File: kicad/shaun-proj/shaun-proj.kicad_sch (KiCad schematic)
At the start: 64 parts, among them J1 USB_C_Receptacle_USB2.0_16P, J2 Conn_02x16_Odd_Even, J3 Conn_01x02_Socket, Q1 AO3401A, Q2 AO3400A, Q3 AO3401A, Q4 AO3400A, Q5 AO3400A, Q6 AO3401A, SW2 SW_SPDT, U1 CH224K, U2 TPS5430DDA, U3 INA219AxD, U5 TP4056-42-ESOP8

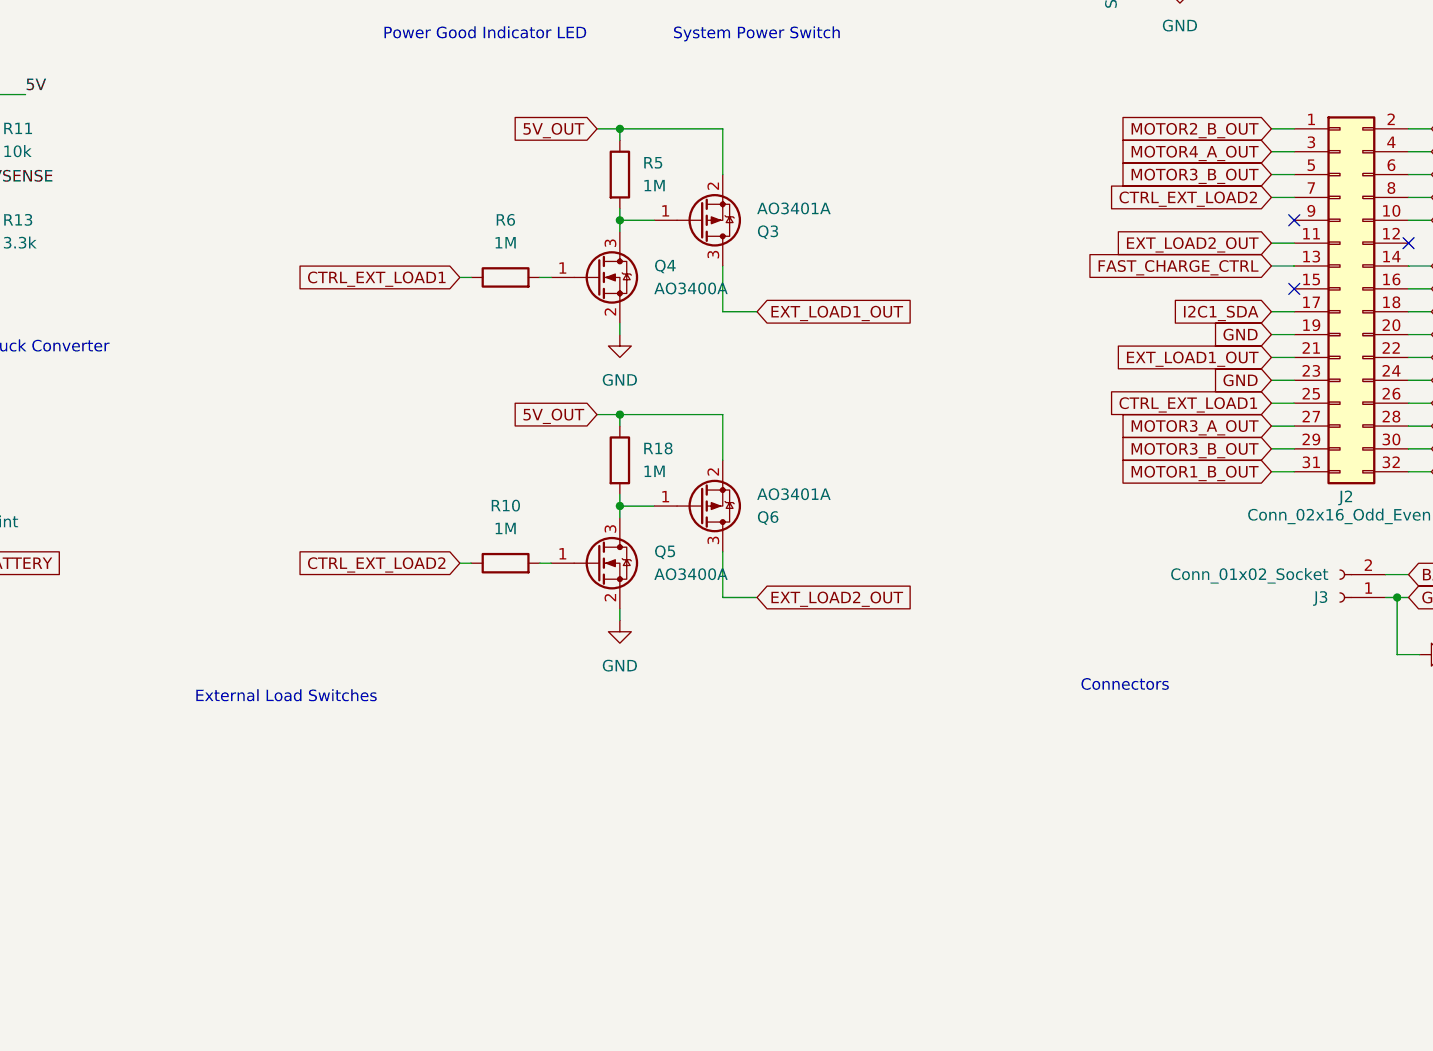
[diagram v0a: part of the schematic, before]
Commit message: combine schematics, optimize damolas schematic, fixes, part assignment, pcb population
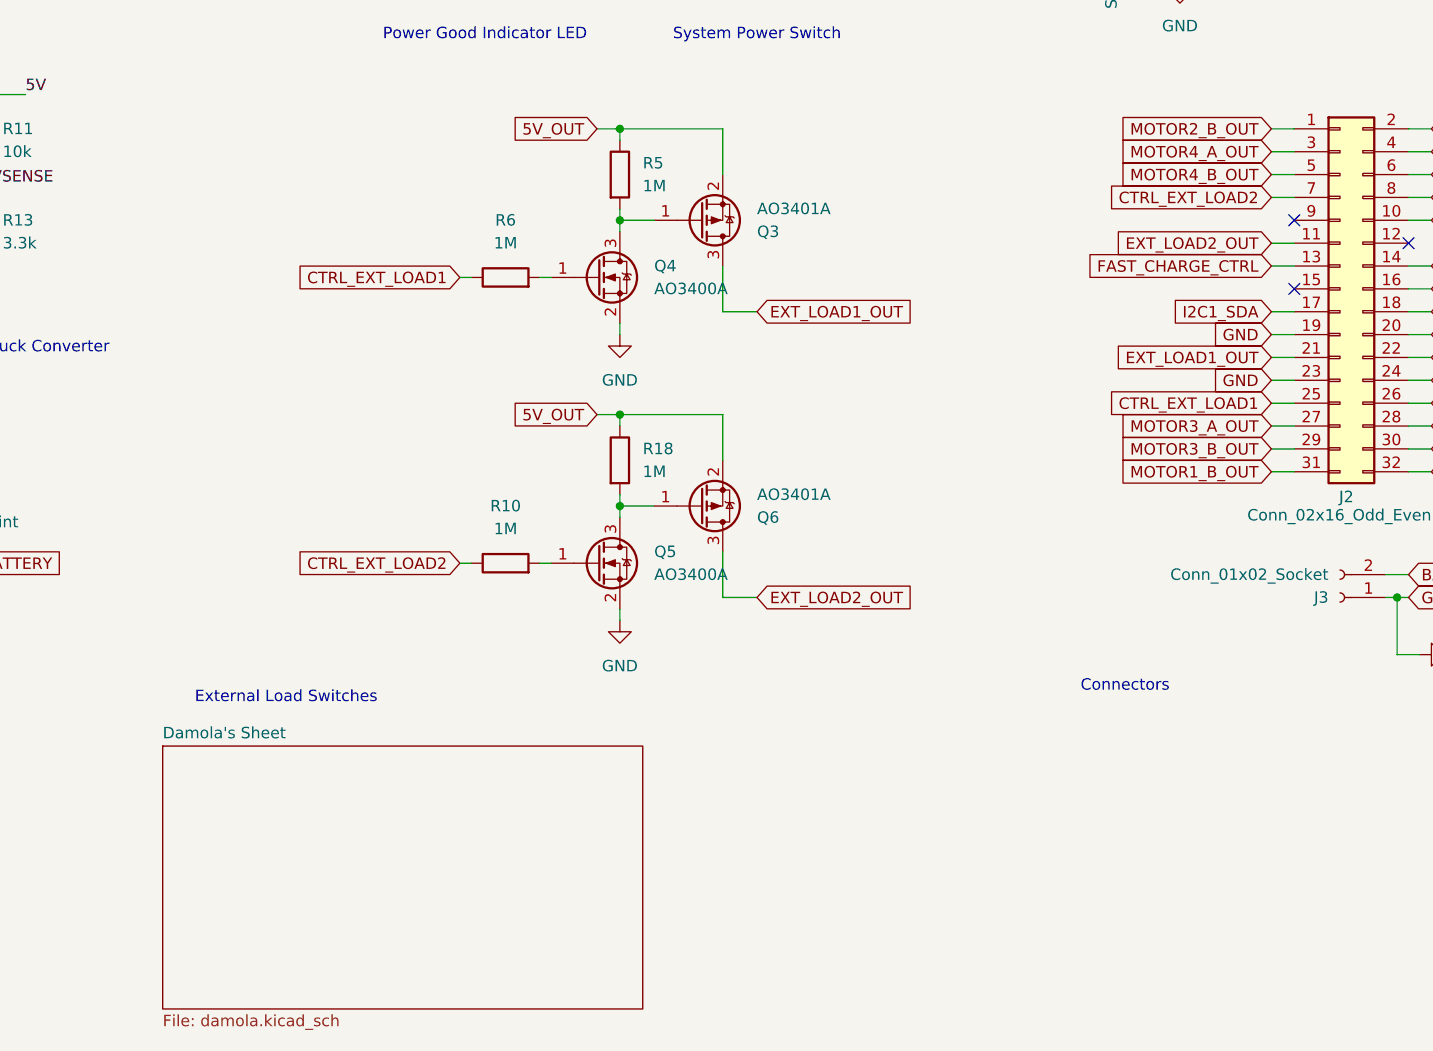
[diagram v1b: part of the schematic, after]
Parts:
- R10, R18, R3, R5, R6: footprint Resistor_SMD:R_0603_1608Metric -> Resistor_SMD:R_0603_1608Metric_Pad0.98x0.95mm_HandSolder
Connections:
- net MOTOR3_B_OUT: no longer J2.5 (Pin_5)
- new net MOTOR4_B_OUT: J2.5 (Pin_5)
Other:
- added sheet Damola's Sheet (damola.kicad_sch)
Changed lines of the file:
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@@
 		)
 	)
-	(global_label "MOTOR3_B_OUT"
+	(global_label "MOTOR4_B_OUT"
 		(shape input)
 		(at 243.84 102.87 180)
@@
 		(polyline
 			(pts
-				(xy 13.97 81.28) (xy 118.11 81.28) (xy 118.11 13.97) (xy 13.97 13.97)
+				(xy 13.97 128.27) (xy 118.11 128.27) (xy 118.11 195.58) (xy 13.97 195.58)
 			)
 			(stroke
@@
 		(polyline
 			(pts
-				(xy 171.45 59.69) (xy 120.65 59.69) (xy 120.65 13.97) (xy 171.45 13.97)
+				(xy 173.99 59.69) (xy 283.21 59.69) (xy 283.21 13.97) (xy 189.23 13.97) (xy 173.99 13.97)
 			)
 			(stroke
@@
 		(polyline
 			(pts
-				(xy 13.97 125.73) (xy 118.11 125.73) (xy 118.11 83.82) (xy 13.97 83.82)
+				(xy 171.45 59.69) (xy 120.65 59.69) (xy 120.65 13.97) (xy 171.45 13.97)
 			)
 			(stroke
@@
 		(polyline
 			(pts
-				(xy 13.97 128.27) (xy 118.11 128.27) (xy 118.11 195.58) (xy 13.97 195.58)
+				(xy 13.97 125.73) (xy 118.11 125.73) (xy 118.11 83.82) (xy 13.97 83.82)
 			)
 			(stroke
@@
 		(polyline
 			(pts
-				(xy 173.99 59.69) (xy 283.21 59.69) (xy 283.21 13.97) (xy 189.23 13.97) (xy 173.99 13.97)
+				(xy 13.97 81.28) (xy 118.11 81.28) (xy 118.11 13.97) (xy 13.97 13.97)
 			)
 			(stroke
@@
 			)
 		)
-		(property "Footprint" "Resistor_SMD:R_0603_1608Metric"
+		(property "Footprint" "Resistor_SMD:R_0603_1608Metric_Pad0.98x0.95mm_HandSolder"
 			(at 169.672 134.62 90)
 			(effects
@@
 			)
 		)
-		(property "Footprint" "Resistor_SMD:R_0603_1608Metric"
+		(property "Footprint" "Resistor_SMD:R_0603_1608Metric_Pad0.98x0.95mm_HandSolder"
 			(at 169.672 102.87 90)
 			(effects
@@
 			)
 		)
-		(property "Footprint" "Resistor_SMD:R_0603_1608Metric"
+		(property "Footprint" "Resistor_SMD:R_0603_1608Metric_Pad0.98x0.95mm_HandSolder"
 			(at 125.222 30.48 90)
 			(effects
@@
 			)
 		)
-		(property "Footprint" "Resistor_SMD:R_0603_1608Metric"
+		(property "Footprint" "Resistor_SMD:R_0603_1608Metric_Pad0.98x0.95mm_HandSolder"
 			(at 158.75 116.078 90)
 			(effects
@@
 			)
 		)
-		(property "Footprint" "Resistor_SMD:R_0603_1608Metric"
+		(property "Footprint" "Resistor_SMD:R_0603_1608Metric_Pad0.98x0.95mm_HandSolder"
 			(at 158.75 147.828 90)
 			(effects
@@
 				)
 			)
+		)
+	)
+	(sheet
+		(at 120.65 166.37)
+		(size 53.34 29.21)
+		(exclude_from_sim no)
+		(in_bom yes)
+		(on_board yes)
+		(dnp no)
+		(fields_autoplaced yes)
+		(stroke
+			(width 0.1524)
+			(type solid)
+		)
+		(fill
+			(color 0 0 0 0.0000)
+		)
+		(property "Sheetname" "Damola's Sheet"
+			(at 120.65 165.6584 0)
+			(effects
+				(font
+					(size 1.27 1.27)
+				)
+				(justify left bottom)
+			)
+		)
+		(property "Sheetfile" "damola.kicad_sch"
+			(at 120.65 196.1646 0)
+			(effects
+				(font
+					(size 1.27 1.27)
+				)
+				(justify left top)
+			)
+		)
+		(instances
+			(project "shaun-proj"
+				(path "/dda18d53-e032-419d-b3dd-4e5b9f14d709"
+					(page "2")
+				)
+			)

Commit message: da board
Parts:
- removed C7: 100n, Capacitor_SMD:C_0603_1608Metric_Pad1.08x0.95mm_HandSolder, symbol Device:C
- removed TP13, TP4, TP5, TP9: TestPoint, TestPoint:TestPoint_Pad_D1.5mm, symbol Connector:TestPoint
- added H1: MountingHole, MountingHole:MountingHole_3.2mm_M3, symbol Mechanical:MountingHole
- R10, R6: value 1M -> 10k
- R4: value 560 -> 2k
- SW2: JLC (none) -> https://jlcpcb.com/partdetail/XkbConnection-SS12D11G3R/C843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
- U1: footprint Package_SO:SSOP-10-1EP_3.9x4.9mm_P1mm_EP2.1x3.3mm -> Package_SO:SSOP-10-1EP_3.9x4.9mm_P1mm_EP2.1x3.3mm_ThermalVias
- U5: footprint Package_SO:SOIC-8-1EP_3.9x4.9mm_P1.27mm_EP2.41x3.3mm -> Package_SO:SOIC-8-1EP_3.9x4.9mm_P1.27mm_EP2.41x3.3mm_ThermalVias; LCSC C9864 -> C16581
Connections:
- net 3V3_OUT: now also J2.17 (Pin_17); no longer J2.18 (Pin_18), R12.1, TP11.1
- net 5V_OUT: now also J2.19 (Pin_19); no longer J2.20 (Pin_20)
- net BATTERY: now also J2.13 (Pin_13), SW2.2 (B); no longer C5.1, J2.14 (Pin_14), SW2.1 (A), TP8.1, U5.5 (BAT)
- net BATTERY_LOAD: now also JP4.2 (B)
- net BATTERY_POWER: now also SW2.3 (C); no longer JP4.2 (B), SW2.2 (B)
- net CTRL_EXT_LOAD1: now also J2.26 (Pin_26); no longer J2.25 (Pin_25)
- net CTRL_EXT_LOAD2: now also J2.8 (Pin_8); no longer J2.7 (Pin_7)
- net EXT_LOAD1_OUT: now also J2.22 (Pin_22); no longer J2.21 (Pin_21)
- net EXT_LOAD2_OUT: now also J2.12 (Pin_12); no longer J2.11 (Pin_11)
- net FAST_CHARGE_CTRL: now also J2.14 (Pin_14); no longer J2.13 (Pin_13)
- net GND: now also J2.20 (Pin_20), J2.24 (Pin_24); no longer J2.19 (Pin_19), J2.23 (Pin_23), SW2.3 (C)
- net HV: now also J2.21 (Pin_21); no longer J2.22 (Pin_22)
- net I2C1_SCL: now also J2.15 (Pin_15); no longer J2.16 (Pin_16)
- net I2C1_SDA: now also J2.18 (Pin_18); no longer J2.17 (Pin_17)
- net MOTOR1_A_OUT: now also J2.31 (Pin_31); no longer J2.32 (Pin_32)
- net MOTOR1_B_OUT: now also J2.32 (Pin_32); no longer J2.31 (Pin_31)
- net MOTOR1_CTRL1: now also J2.27 (Pin_27); no longer J2.28 (Pin_28)
- net MOTOR1_CTRL2: now also J2.29 (Pin_29); no longer J2.30 (Pin_30)
- net MOTOR2_A_OUT: now also J2.1 (Pin_1); no longer J2.2 (Pin_2)
- net MOTOR2_B_OUT: now also J2.2 (Pin_2); no longer J2.1 (Pin_1)
- net MOTOR2_CTRL1: now also J2.3 (Pin_3); no longer J2.4 (Pin_4)
- net MOTOR2_CTRL2: now also J2.5 (Pin_5); no longer J2.6 (Pin_6)
- net MOTOR3_A_OUT: now also J2.28 (Pin_28); no longer J2.27 (Pin_27)
- net MOTOR3_B_OUT: now also J2.30 (Pin_30); no longer J2.29 (Pin_29)
- net MOTOR3_CTRL1: now also J2.23 (Pin_23); no longer J2.24 (Pin_24)
- net MOTOR3_CTRL2: now also J2.25 (Pin_25); no longer J2.26 (Pin_26)
- net MOTOR4_A_OUT: now also J2.4 (Pin_4); no longer J2.3 (Pin_3)
- net MOTOR4_B_OUT: now also J2.6 (Pin_6); no longer J2.5 (Pin_5)
- net MOTOR4_CTRL1: now also J2.7 (Pin_7); no longer J2.8 (Pin_8)
- net MOTOR4_CTRL2: now also J2.9 (Pin_9); no longer J2.10 (Pin_10)
- net at JP4.1 (A), JP5.2 (B), U3.5 (VS): now also R12.1, TP11.1
- new net CHARGE_BATTERY: C5.1, SW2.1 (A), TP8.1, U5.5 (BAT)
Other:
- moved on the sheet: C3, J3, JP5, R16, R8, SW2
